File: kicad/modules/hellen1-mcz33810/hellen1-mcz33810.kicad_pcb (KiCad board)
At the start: 4 copper layers, 44.8 x 12.5 mm, 32 parts, among them M801 Module-mcz33810-0.1, Q801 ISL9V3040D3S, Q802 ISL9V3040D3S, Q803 ISL9V3040D3S, Q804 ISL9V3040D3S, U801 MCZ33810EK

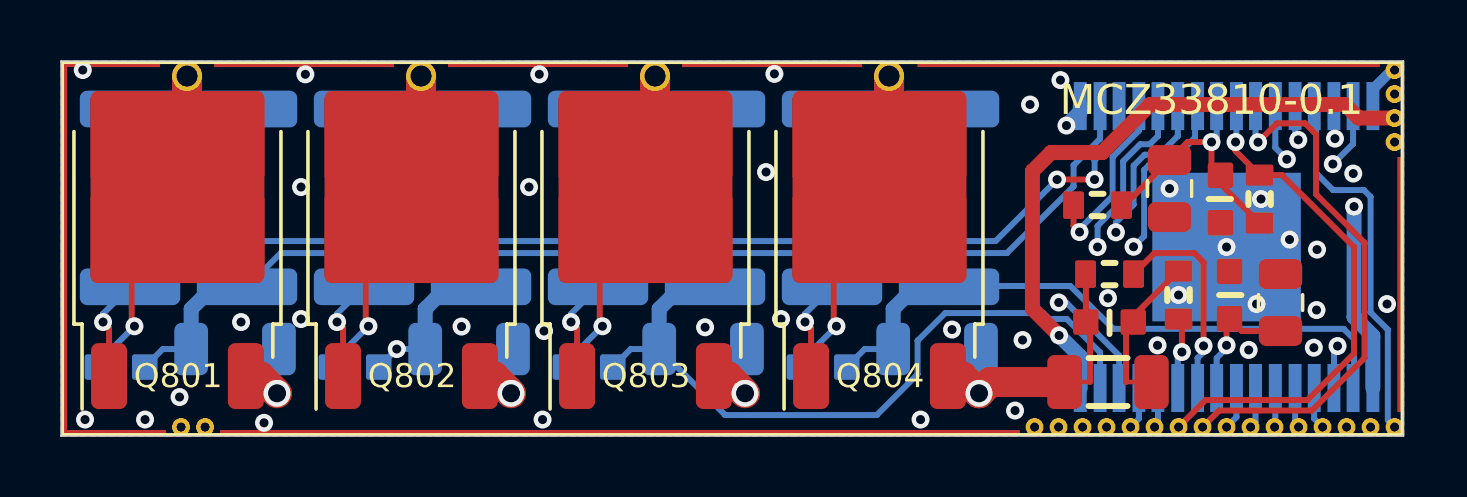
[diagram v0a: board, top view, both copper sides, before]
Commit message: Upd mcz33810 borders #376
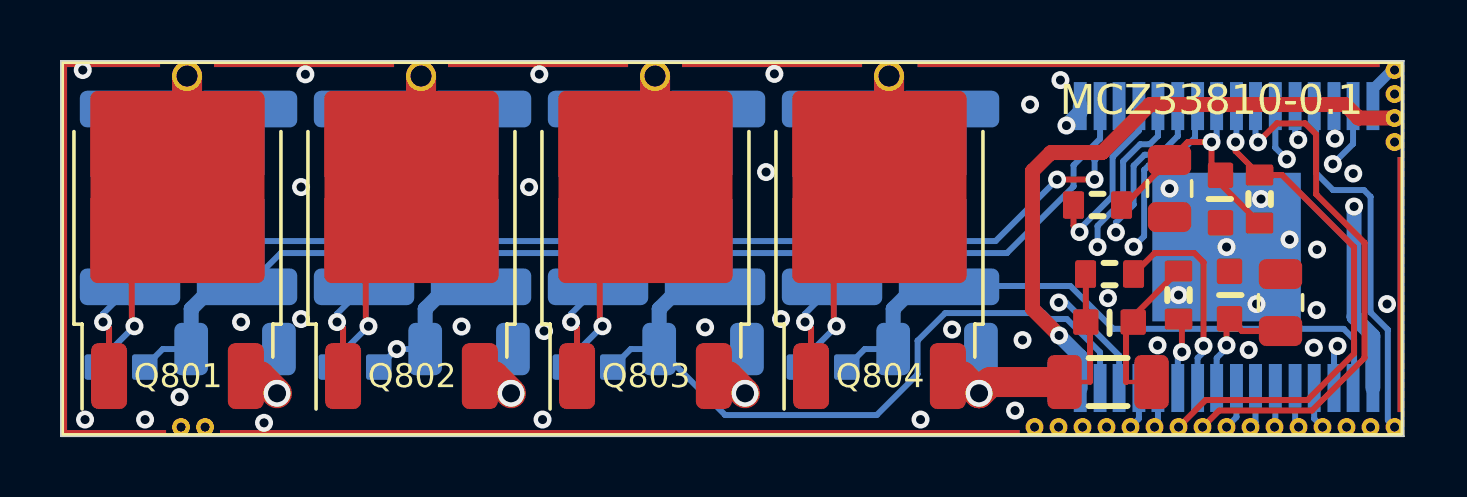
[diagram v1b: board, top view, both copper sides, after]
